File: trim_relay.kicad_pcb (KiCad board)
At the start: 2 copper layers, 26 parts, among them K1 G5Q-1, K2 G5Q-1, K3 G5Q-1, K4 G5Q-1, K5 G5Q-1, Q1 2N3906, Q2 2N3904, Q3 2N3904, Q4 2N3904, Q5 2N3904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

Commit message: pcb completed
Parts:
- added J1: Conn_01x01, CustomComponents:FASTON-187-vert-90deg-terminal, F.Cu at (45.5, 56.5)
- added J10: Conn_01x01, CustomComponents:FASTON-187-vert-90deg-terminal, F.Cu at (45.5, 92.5)
- added J11: Conn_01x01, CustomComponents:FASTON-187-vert-90deg-terminal, F.Cu at (45.5, 97.0)
- added J2: Conn_01x01, CustomComponents:FASTON-187-vert-90deg-terminal, F.Cu at (45.5, 70.0)
- added J3: Conn_01x01, CustomComponents:FASTON-187-vert-90deg-terminal, F.Cu at (45.5, 52.0)
- added J4: Conn_01x01, CustomComponents:FASTON-187-vert-90deg-terminal, F.Cu at (45.5, 65.5)
- added J5: Conn_01x01, CustomComponents:FASTON-187-vert-90deg-terminal, F.Cu at (45.5, 61.0)
- added J6: Conn_01x01, CustomComponents:FASTON-187-vert-90deg-terminal, F.Cu at (45.5, 74.5)
- added J7: Conn_01x01, CustomComponents:FASTON-187-vert-90deg-terminal, F.Cu at (45.5, 79.0)
- added J8: Conn_01x01, CustomComponents:FASTON-187-vert-90deg-terminal, F.Cu at (45.5, 83.5)
- added J9: Conn_01x01, CustomComponents:FASTON-187-vert-90deg-terminal, F.Cu at (45.5, 88.0)
- added REF**: MountingHole_3mm, Mounting_Holes:MountingHole_3mm, F.Cu at (43.5, 43.5)
- added REF**: MountingHole_3mm, Mounting_Holes:MountingHole_3mm, F.Cu at (111.5, 43.5)
- added REF**: MountingHole_3mm, Mounting_Holes:MountingHole_3mm, F.Cu at (43.5, 111.5)
- added REF**: MountingHole_3mm, Mounting_Holes:MountingHole_3mm, F.Cu at (111.5, 111.5)
- D1, D2, D3, D4, D5: footprint Diodes_THT:D_DO-41_SOD81_P7.62mm_Horizontal -> Diodes_THT:D_DO-41_SOD81_P10.16mm_Horizontal
- K1, K2, K3, K4, K5: value G5Q-1 -> G5LE; footprint Relays_THT:Relay_SPDT_OMRON-G5Q -> Relays_THT:Relay_SPDT_OMRON-G5LE-1
- R1, R2, R3, R4, R5, R6, R7: footprint Resistors_THT:R_Axial_DIN0414_L11.9mm_D4.5mm_P15.24mm_Horizontal -> Resistors_THT:R_Axial_DIN0207_L6.3mm_D2.5mm_P10.16mm_Horizontal
- U1: footprint TO_SOT_Packages_THT:TO-92_Inline_Narrow_Oval -> TO_SOT_Packages_THT:TO-92_Horizontal2_Inline_Narrow_Oval
- moved C1 169.3 mm to (58.0, 102.0), turned to 270 degrees
- moved C2 169.2 mm to (58.0, 109.0), turned to 270 degrees
- moved Q3 146.3 mm to (109.5, 54.0), turned to 270 degrees
- moved Q2 128.9 mm to (109.5, 75.5), turned to 270 degrees
- moved K3 128.0 mm to (82.0, 53.0), turned to 90 degrees
- moved Q1 126.6 mm to (105.0, 86.0), turned to 270 degrees
- moved K4 114.2 mm to (54.5, 53.0), turned to 90 degrees
- moved D4 114.1 mm to (63.5, 42.5), turned to 180 degrees
- moved U1 113.4 mm to (66.0, 101.5), turned to 180 degrees
- moved R5 110.4 mm to (77.0, 56.0), turned to 90 degrees
- moved Q5 107.0 mm to (70.0, 87.5)
- moved K5 103.5 mm to (54.5, 75.0), turned to 90 degrees
- moved Q4 102.5 mm to (62.5, 87.5)
- moved R6 102.1 mm to (77.0, 78.0), turned to 90 degrees
- moved D5 101.7 mm to (63.5, 64.0), turned to 180 degrees
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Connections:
- C2 pad 1: Net-(C2-Pad1) -> V_ADJ
- K1 pad 1: Net-(D1-Pad1) -> V_ELEV
- K1 pad 2: V_ELEV -> GND
- K1 pad 5: GND -> Net-(D1-Pad1)
- K2 pad 1: Net-(D2-Pad2) -> TRIM_AL_UP_OUT
- K2 pad 2: TRIM_AL_UP_OUT -> +12V
- K2 pad 5: +12V -> Net-(D2-Pad2)
- K3 pad 1: Net-(D3-Pad2) -> TRIM_AL_DN_OUT
- K3 pad 2: TRIM_AL_DN_OUT -> +12V
- K3 pad 5: +12V -> Net-(D3-Pad2)
- K4 pad 1: Net-(D4-Pad2) -> TRIM_ELEV_UP_OUT
- K4 pad 2: TRIM_ELEV_UP_OUT -> +12V
- K4 pad 5: +12V -> Net-(D4-Pad2)
- K5 pad 1: Net-(D5-Pad2) -> TRIM_ELEV_DN_OUT
- K5 pad 2: TRIM_ELEV_DN_OUT -> +12V
- K5 pad 5: +12V -> Net-(D5-Pad2)
- R7 pad 2: Net-(C2-Pad1) -> V_ADJ
- U1 pad 2: Net-(C2-Pad1) -> V_ADJ
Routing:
- net +12V: track 0.00 -> 222.2 mm
- net FLAP_DN: track 0.00 -> 91.9 mm
- net TRIM_AL_DN_IN: track 0.00 -> 84.2 mm, vias 0 -> 1
- net Net-(D5-Pad2): track 0.00 -> 69.2 mm, vias 0 -> 1
- net TRIM_AL_UP_IN: track 0.00 -> 68.7 mm
- net V_ELEV: track 0.00 -> 56.3 mm, vias 0 -> 1
- net TRIM_ELEV_UP_IN: track 0.00 -> 51.7 mm
- net V_ADJ: track 0.00 -> 50.0 mm
- net Net-(D4-Pad2): track 0.00 -> 49.8 mm, vias 0 -> 1
- net TRIM_ELEV_DN_IN: track 0.00 -> 49.3 mm, vias 0 -> 1
- net TRIM_AL_UP_OUT: track 0.00 -> 43.0 mm
- net Net-(Q4-Pad2): track 0.00 -> 41.5 mm, vias 0 -> 2
- net TRIM_AL_DN_OUT: track 0.00 -> 41.1 mm
- net Net-(D2-Pad2): track 0.00 -> 36.4 mm
- net Net-(D3-Pad2): track 0.00 -> 36.4 mm
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- added copper zone on B.Cu, net GND
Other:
- board outline added: 75 x 75 mm
- board text added: "12V"
- board text added: "AL-DN-IN"
- board text added: "AL-DN-OUT"
- board text added: "AL-UP-IN"
- board text added: "AL-UP-OUT"
- board text added: "EL-DN-IN"
- board text added: "EL-DN-OUT"
- board text added: "EL-UP-IN"
- board text added: "EL-UP-OUT"
- board text added: "FLAP-DN"
- board text added: "GND"

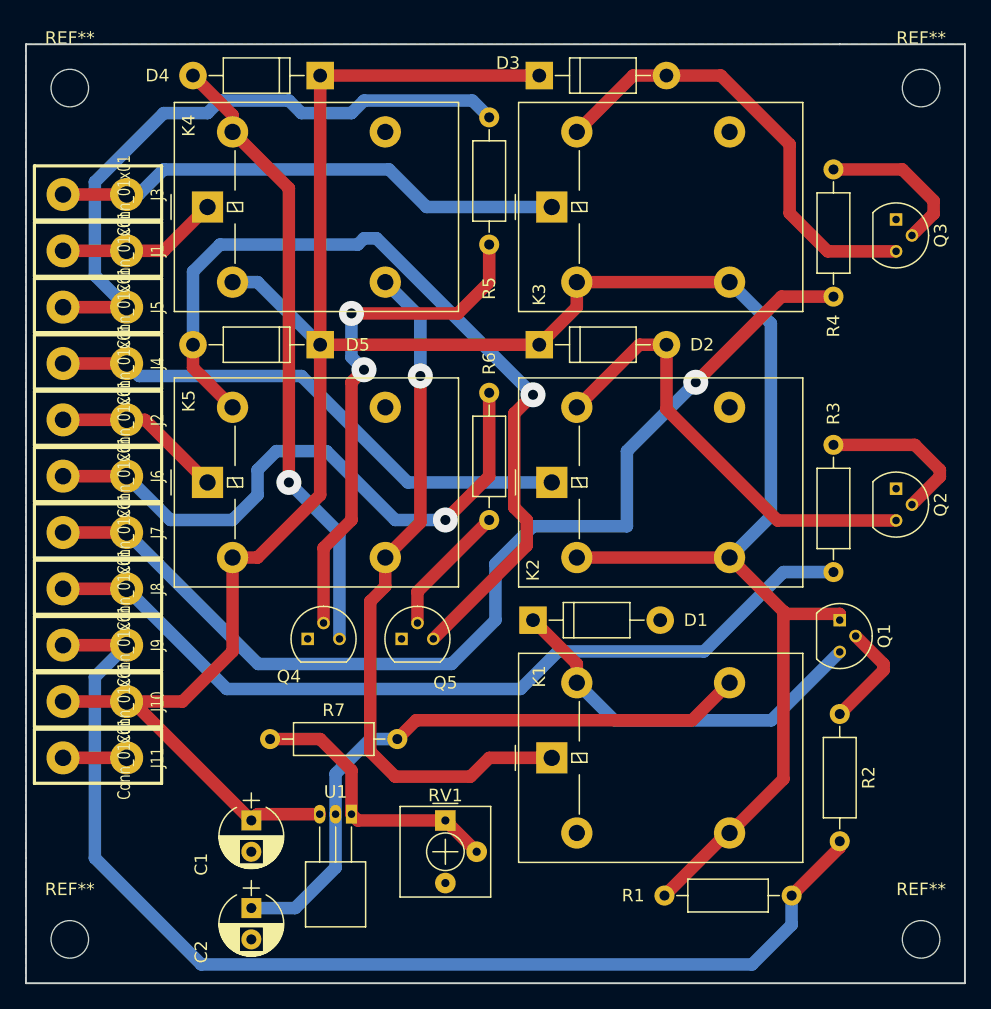
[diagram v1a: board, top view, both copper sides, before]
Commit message: Changed all inputs to grounding for active
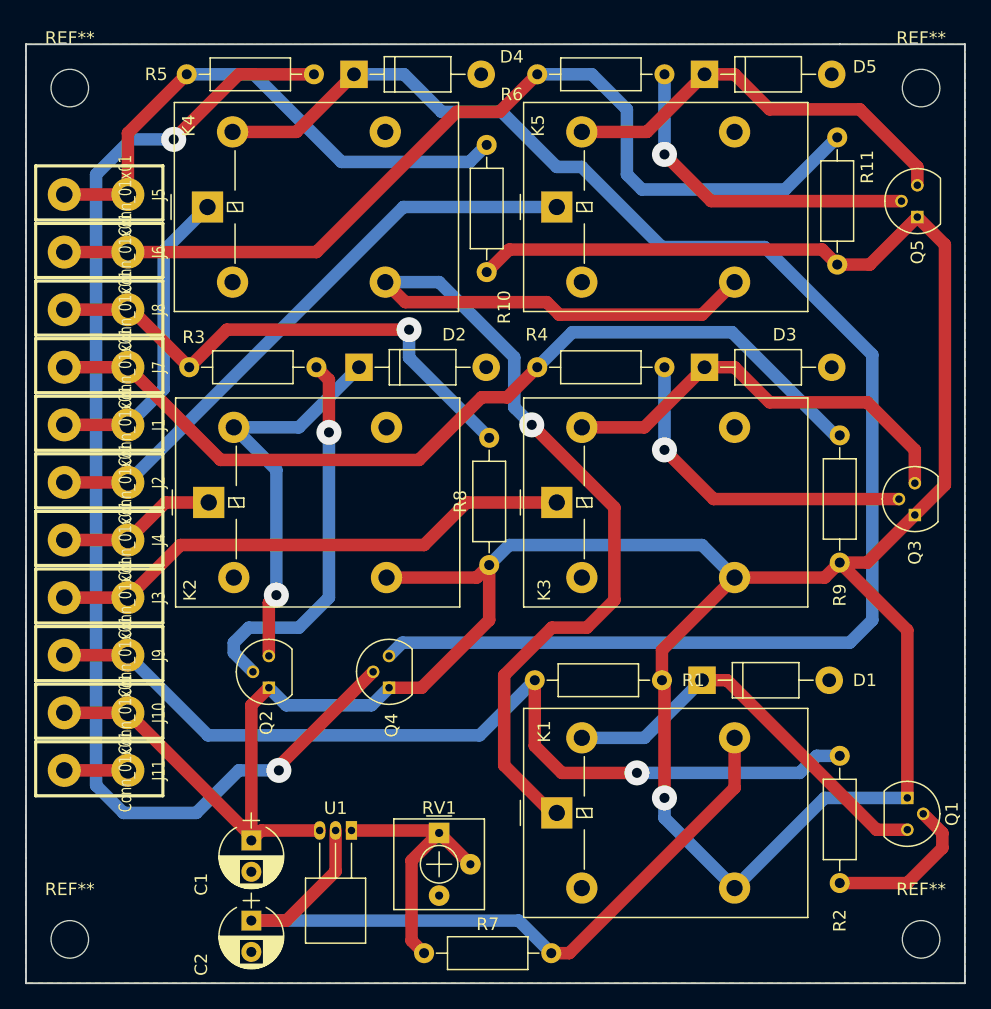
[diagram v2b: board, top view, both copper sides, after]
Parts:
- added R10: R, Resistors_THT:R_Axial_DIN0207_L6.3mm_D2.5mm_P10.16mm_Horizontal, F.Cu at (76.8, 58.2)
- added R11: R, Resistors_THT:R_Axial_DIN0207_L6.3mm_D2.5mm_P10.16mm_Horizontal, F.Cu at (104.8, 57.6)
- added R8: R, Resistors_THT:R_Axial_DIN0207_L6.3mm_D2.5mm_P10.16mm_Horizontal, F.Cu at (77.0, 81.6)
- added R9: R, Resistors_THT:R_Axial_DIN0207_L6.3mm_D2.5mm_P10.16mm_Horizontal, F.Cu at (105.0, 81.4)
- Q2, Q3, Q4, Q5: value 2N3904 -> 2N3906
- moved Q5 53.2 mm to (111.2, 53.8), turned to 90 degrees
- moved Q2 52.6 mm to (59.4, 91.4), turned to 90 degrees
- moved R3 41.8 mm to (63.2, 65.8), turned to 180 degrees
- moved R6 38.3 mm to (91.0, 42.4), turned to 180 degrees
- moved D5 37.5 mm to (94.2, 42.4), turned to 0 degrees
- moved K5 35.5 mm to (82.4, 53.0)
- moved J3 32.2 mm to (45.6, 84.2)
- moved K2 27.4 mm to (54.6, 76.6)
- moved D3 26.8 mm to (94.2, 65.8)
- moved Q3 23.6 mm to (111.0, 77.6), turned to 90 degrees
- moved K3 23.6 mm to (82.4, 76.6)
- moved J8 22.3 mm to (45.6, 61.2)
- moved R7 21.1 mm to (71.8, 112.6)
- moved R4 20.8 mm to (91.0, 65.8), turned to 180 degrees
- moved R5 19.5 mm to (63.0, 42.4), turned to 180 degrees
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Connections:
- D2 pad 1: +12V -> Net-(D2-Pad1)
- D2 pad 2: Net-(D2-Pad2) -> GND
- D3 pad 1: +12V -> Net-(D3-Pad1)
- D3 pad 2: Net-(D3-Pad2) -> GND
- D4 pad 1: +12V -> Net-(D4-Pad1)
- D4 pad 2: Net-(D4-Pad2) -> GND
- D5 pad 1: +12V -> Net-(D5-Pad1)
- D5 pad 2: Net-(D5-Pad2) -> GND
- K2 pad 2: +12V -> GND
- K2 pad 5: Net-(D2-Pad2) -> Net-(D2-Pad1)
- K3 pad 2: +12V -> GND
- K3 pad 5: Net-(D3-Pad2) -> Net-(D3-Pad1)
- K4 pad 2: +12V -> GND
- K4 pad 5: Net-(D4-Pad2) -> Net-(D4-Pad1)
- K5 pad 2: +12V -> GND
- K5 pad 5: Net-(D5-Pad2) -> Net-(D5-Pad1)
- Q2 pad 1: GND -> +12V
- Q2 pad 3: Net-(D2-Pad2) -> Net-(D2-Pad1)
- Q3 pad 1: GND -> +12V
- Q3 pad 3: Net-(D3-Pad2) -> Net-(D3-Pad1)
- Q4 pad 1: GND -> +12V
- Q4 pad 3: Net-(D4-Pad2) -> Net-(D4-Pad1)
- Q5 pad 1: GND -> +12V
- Q5 pad 3: Net-(D5-Pad2) -> Net-(D5-Pad1)
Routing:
- net Net-(D4-Pad1): track 0.00 -> 123.3 mm
- net Net-(D5-Pad2): track 69.2 -> 0.00 mm, vias 1 -> 0
- net Net-(Q4-Pad2): track 41.5 -> 97.4 mm
- net Net-(D4-Pad2): track 49.8 -> 0.00 mm, vias 1 -> 0
- net Net-(D2-Pad2): track 36.4 -> 0.00 mm
- net Net-(D3-Pad2): track 36.4 -> 0.00 mm
- net TRIM_ELEV_DN_OUT: track 13.6 -> 48.5 mm
- net Net-(D3-Pad1): track 0.00 -> 34.0 mm
- net V_ELEV: track 56.3 -> 89.8 mm
- net Net-(D5-Pad1): track 0.00 -> 33.2 mm
- net Net-(D2-Pad1): track 0.00 -> 31.9 mm, vias 0 -> 1
- net TRIM_AL_UP_OUT: track 43.0 -> 12.8 mm
- net TRIM_ELEV_DN_IN: track 49.3 -> 76.2 mm, vias 1 -> 0
- net TRIM_AL_UP_IN: track 68.7 -> 42.0 mm, vias 0 -> 1
- net FLAP_DN: track 91.9 -> 73.1 mm, vias 0 -> 1
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
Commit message: Fixed layout
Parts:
- C1, C2: value CP -> 0.68uF
- K1, K2, K3, K4, K5: value G5LE -> G5Q-14 DC12; footprint Relays_THT:Relay_SPDT_OMRON-G5LE-1 -> Relays_THT:Relay_SPDT_OMRON-G5Q
- Q1, Q2, Q3, Q4, Q5: footprint TO_SOT_Packages_THT:TO-92_Molded_Narrow -> TO_SOT_Packages_THT:TO-92_Inline_Wide
- R1, R10, R11, R8, R9: value R -> 10K
- R2, R3, R4, R5, R6: value R -> 3K9
- R7: value R -> 120
- RV1: value POT -> 1K
- moved Q4 31.3 mm to (73.8, 60.5), turned to 180 degrees
- moved R2 25.5 mm to (87.0, 89.0), turned to 0 degrees
- moved R1 18.3 mm to (105.2, 102.0), turned to 90 degrees
- moved D4 17.9 mm to (64.8, 60.2), turned to 180 degrees
- moved D5 17.9 mm to (92.8, 60.2), turned to 180 degrees
- moved D3 17.5 mm to (92.5, 83.2), turned to 180 degrees
- moved D2 17.3 mm to (64.5, 83.0), turned to 180 degrees
- moved Q2 16.4 mm to (73.8, 83.5), turned to 180 degrees
- moved D1 14.8 mm to (92.5, 105.5), turned to 180 degrees
- moved R7 12.2 mm to (69.0, 100.8)
- moved Q5 11.6 mm to (101.8, 60.5), turned to 180 degrees
- moved C1 11.4 mm to (57.0, 92.2)
- moved U1 11.3 mm to (65.5, 91.5)
- moved RV1 11.3 mm to (72.8, 91.8)
- moved Q3 11.0 mm to (101.8, 83.5), turned to 180 degrees
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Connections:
- K1 pad 1: V_ELEV -> Net-(D1-Pad1)
- K1 pad 2: GND -> V_ELEV
- K1 pad 5: Net-(D1-Pad1) -> GND
- K2 pad 1: TRIM_AL_UP_OUT -> Net-(D2-Pad1)
- K2 pad 2: GND -> TRIM_AL_UP_OUT
- K2 pad 5: Net-(D2-Pad1) -> GND
- K3 pad 1: TRIM_AL_DN_OUT -> Net-(D3-Pad1)
- K3 pad 2: GND -> TRIM_AL_DN_OUT
- K3 pad 5: Net-(D3-Pad1) -> GND
- K4 pad 1: TRIM_ELEV_UP_OUT -> Net-(D4-Pad1)
- K4 pad 2: GND -> TRIM_ELEV_UP_OUT
- K4 pad 5: Net-(D4-Pad1) -> GND
- K5 pad 1: TRIM_ELEV_DN_OUT -> Net-(D5-Pad1)
- K5 pad 2: GND -> TRIM_ELEV_DN_OUT
- K5 pad 5: Net-(D5-Pad1) -> GND
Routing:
- net Net-(D4-Pad1): track 123.3 -> 15.7 mm
- net Net-(Q4-Pad2): track 97.4 -> 22.8 mm, vias 2 -> 0
- net +12V: track 240.1 -> 169.1 mm
- net TRIM_ELEV_UP_OUT: track 25.1 -> 49.9 mm
- net Net-(D3-Pad1): track 34.0 -> 15.8 mm
- net Net-(D5-Pad1): track 33.2 -> 15.8 mm
- net Net-(D1-Pad1): track 32.9 -> 15.5 mm
- net Net-(D2-Pad1): track 31.9 -> 15.9 mm, vias 1 -> 0
- net TRIM_ELEV_DN_OUT: track 48.5 -> 63.6 mm, vias 0 -> 1
- net TRIM_AL_DN_OUT: track 42.5 -> 54.5 mm, vias 0 -> 1
- net TRIM_AL_UP_OUT: track 12.8 -> 24.4 mm
- net Net-(Q1-Pad2): track 12.7 -> 21.7 mm
- net FLAP_DN: track 73.1 -> 65.1 mm
- net Net-(Q2-Pad2): track 30.9 -> 23.3 mm, vias 1 -> 0
- net TRIM_ELEV_DN_IN: track 76.2 -> 69.4 mm
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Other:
- board size 75 x 75 mm -> 75 x 71 mm
- board text added: "www-bit-builder.com-trim_relay-v1.0"

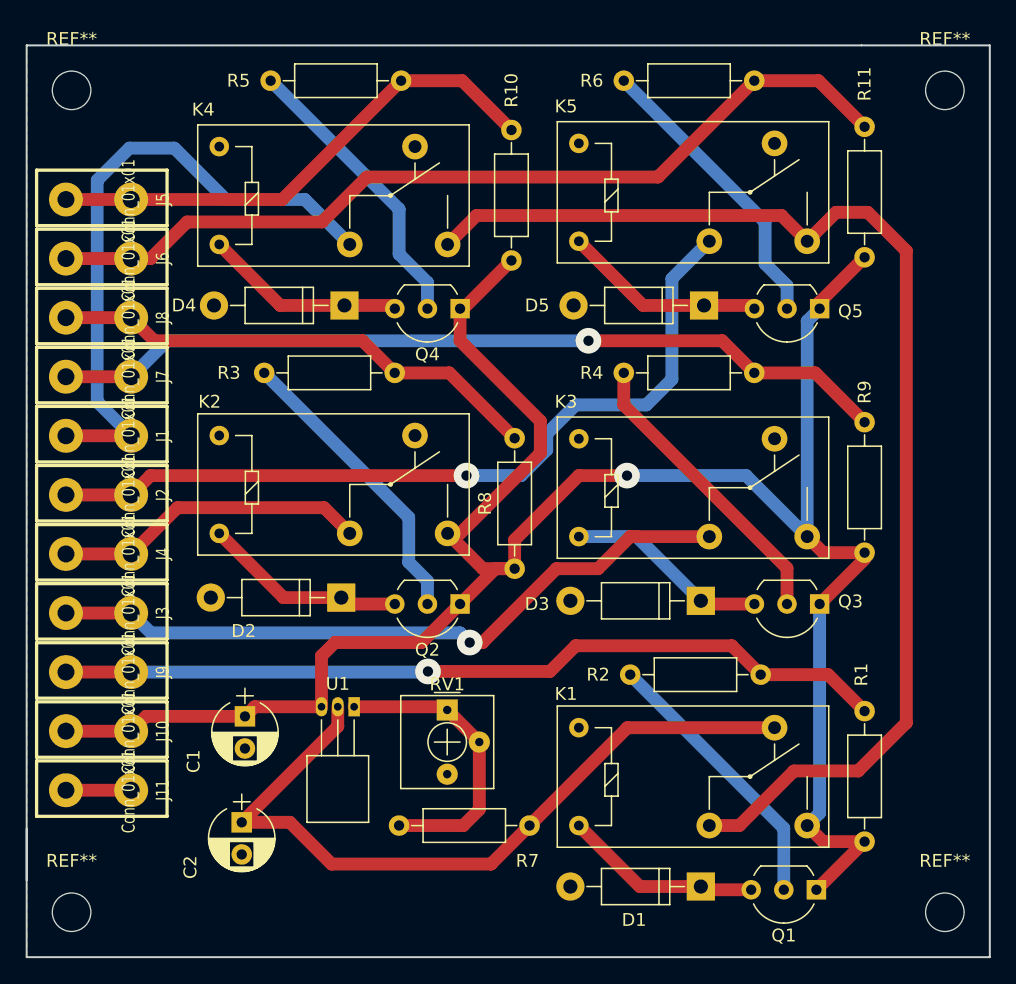
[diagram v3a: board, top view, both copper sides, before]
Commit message: Switch 1 power supply to 1 for each system
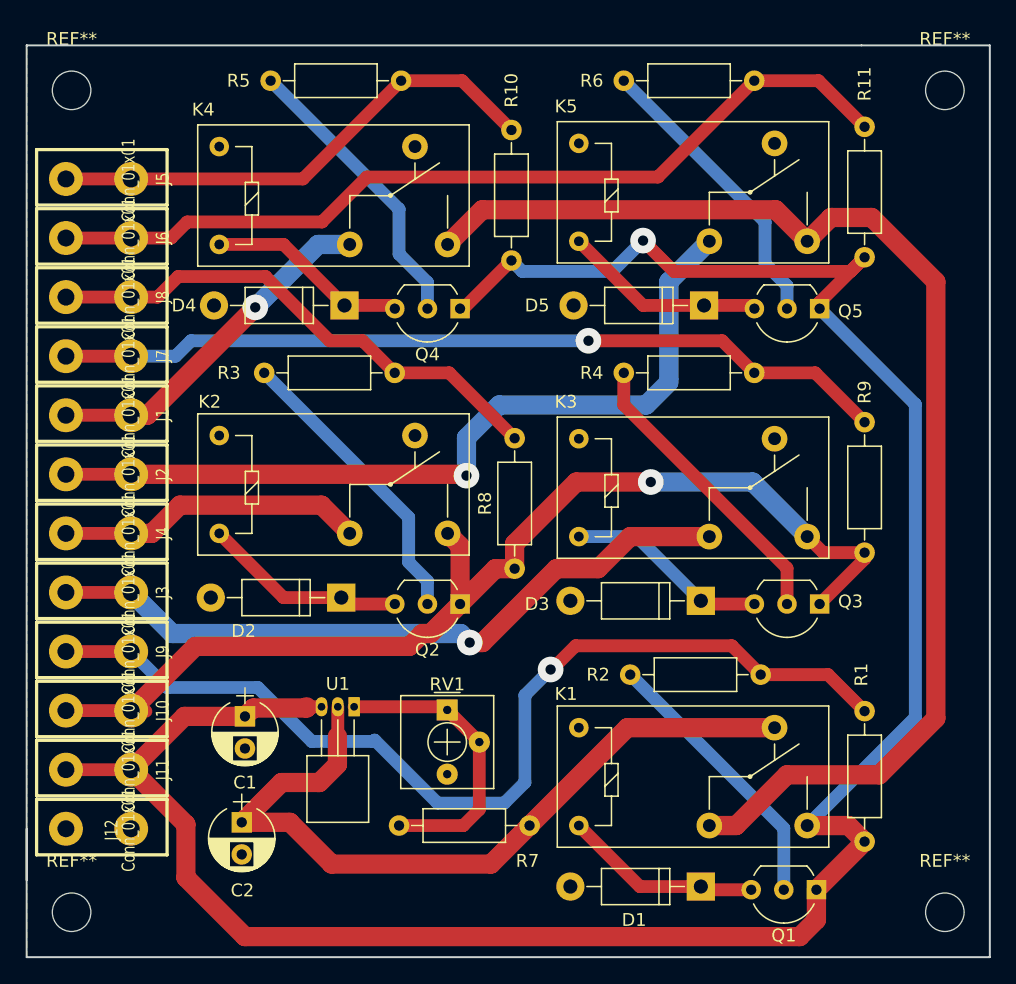
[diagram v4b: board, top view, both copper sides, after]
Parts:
- added J12: Conn_01x01, CustomComponents:FASTON-187-vert-90deg-terminal, F.Cu at (45.6, 101.0)
- moved J1 1.60 mm to (45.6, 68.8)
- moved J10 1.60 mm to (45.6, 91.8)
- moved J3 1.60 mm to (45.6, 82.6)
- moved J5 1.60 mm to (45.6, 50.4)
- moved J6 1.60 mm to (45.6, 55.0)
- moved J8 1.60 mm to (45.6, 59.6)
- moved J11 1.60 mm to (45.6, 96.4)
- moved J2 1.60 mm to (45.6, 73.4)
- moved J4 1.60 mm to (45.6, 78.0)
- moved J7 1.60 mm to (45.6, 64.2)
- moved J9 1.60 mm to (45.6, 87.2)
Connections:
- C1 pad 1: +12V -> VDD
- J10 pad 1: +12V -> VCC
- J11 pad 1: GND -> VDD
- K1 pad 3: +12V -> VDD
- K2 pad 3: +12V -> VCC
- K3 pad 3: +12V -> VCC
- Q1 pad 1: +12V -> VDD
- Q2 pad 1: +12V -> VCC
- Q3 pad 1: +12V -> VCC
- Q4 pad 1: +12V -> VDD
- Q5 pad 1: +12V -> VDD
- R1 pad 1: +12V -> VDD
- R10 pad 1: +12V -> VDD
- R11 pad 1: +12V -> VDD
- R8 pad 1: +12V -> VCC
- R9 pad 1: +12V -> VCC
- U1 pad 3: +12V -> VDD
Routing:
- net VDD: track 0.00 -> 189.6 mm, vias 0 -> 1
- net +12V: track 169.1 -> 0.00 mm, vias 1 -> 0
- net VCC: track 0.00 -> 86.1 mm, vias 0 -> 1
- net V_ADJ: track 59.3 -> 104.5 mm
- net TRIM_AL_DN_OUT: track 54.5 -> 99.0 mm
- net TRIM_ELEV_UP_OUT: track 49.9 -> 27.6 mm, vias 0 -> 1
- net TRIM_AL_UP_OUT: track 24.4 -> 41.0 mm
- net TRIM_ELEV_DN_OUT: track 63.6 -> 78.8 mm
- net FLAP_DN: track 65.1 -> 78.6 mm
- net GND: track 5.08 -> 0.00 mm
- net V_ELEV: track 95.1 -> 98.1 mm
- net TRIM_AL_UP_IN: track 38.8 -> 41.1 mm
- net TRIM_ELEV_UP_IN: track 40.1 -> 39.4 mm
- net TRIM_ELEV_DN_IN: track 69.4 -> 68.8 mm
- net TRIM_AL_DN_IN: track 66.0 -> 65.3 mm
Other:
- board text added: "12V-AILERON"
- board text added: "12V-ELEVATOR"
- board text removed: "12V"
